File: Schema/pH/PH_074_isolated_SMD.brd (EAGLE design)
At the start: 67 x 48 mm, 31 parts, among them IC1 TL074D, IC2 TLC271D

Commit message: update pH schema and board
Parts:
- added R13: 1k, rcl:R1206W
- R8: device rcl:R0805W -> rcl:R1206W
- moved PWS1 11.4 mm to (64.7, 17.1), flipped to the top, turned to 180 degrees
- moved LED1 5.55 mm to (47.3, 7.80), turned to 180 degrees
- moved R6 5.40 mm to (47.3, 11.9)
- moved R5 5.40 mm to (45.2, 11.9)
- moved U$1 4.27 mm to (53.9, 23.2), turned to 270 degrees
- moved IL300 2.60 mm to (46.1, 26.3)
- moved TRIM1 1.00 mm to (35.5, 35.0)
- moved TRIM2 1.00 mm to (35.5, 13.0)
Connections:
- new net NIC: C7.1, IC2.6, R11.1, R13.2
- net GND: now also LED1.A
- net N$1: now also TRIM2.2; no longer TRIM2.1
- net N$12: now also TRIM1.2; no longer TRIM1.1
- net OUTPUT: now also R13.1; no longer C7.1, IC2.6, R11.1
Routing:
- net NIC: track 0.00 -> 16.8 mm
- net OUTPUT: track 19.9 -> 4.30 mm
- net +12V: track 90.6 -> 80.6 mm
- net +5V: track 16.8 -> 9.19 mm
- net N$1: track 26.7 -> 33.7 mm
- net N$7: track 35.4 -> 41.8 mm
- net -12V: track 49.6 -> 45.7 mm
- net N$8: track 10.7 -> 13.7 mm
- net N$21: track 23.4 -> 20.6 mm
- net N$9: track 5.70 -> 8.43 mm
- net N$12: track 21.1 -> 23.5 mm
- net N$4: track 19.8 -> 21.2 mm
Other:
- board text added: "+"
- board text added: "-"
- board text added: "GAIN"
- board text added: "OFFSET"
- board text added: "by Sensuino"
- board text added: "pH"
- board text added: "pH rev 1.1"

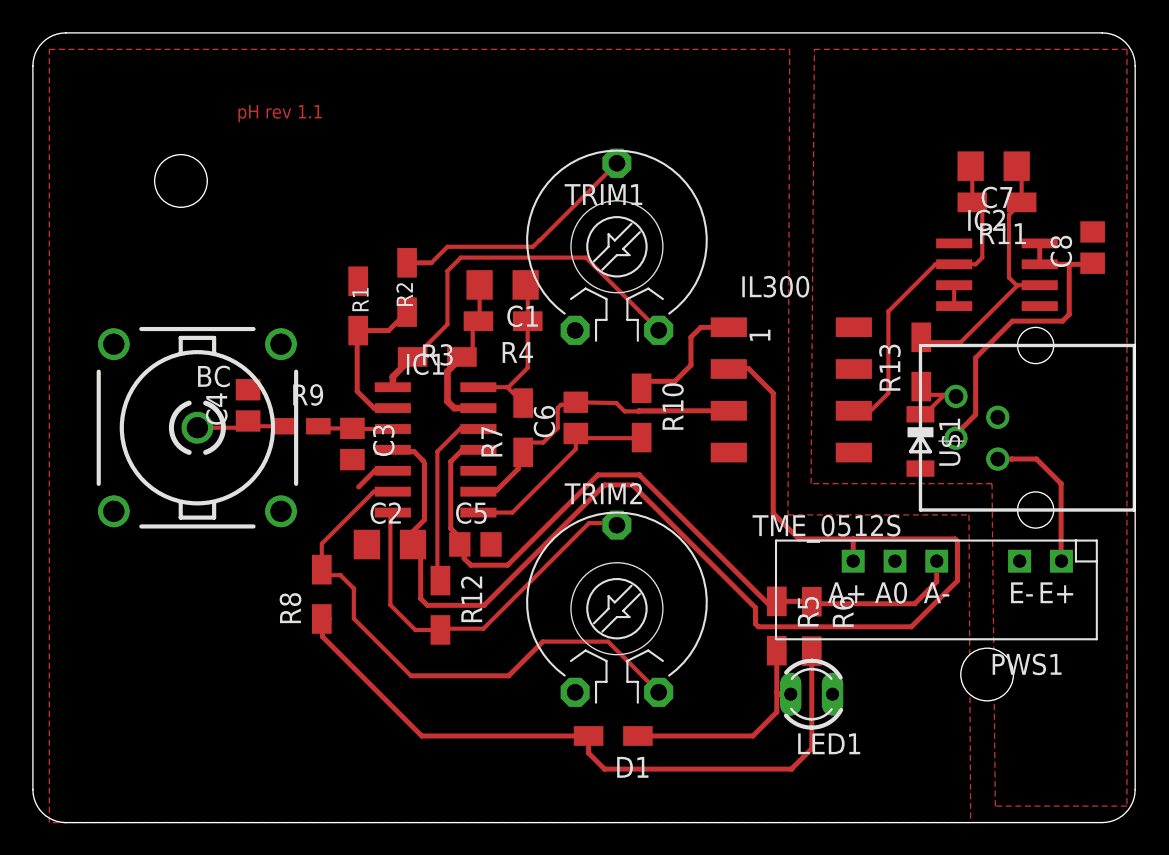
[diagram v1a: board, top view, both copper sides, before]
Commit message: little board adjustment
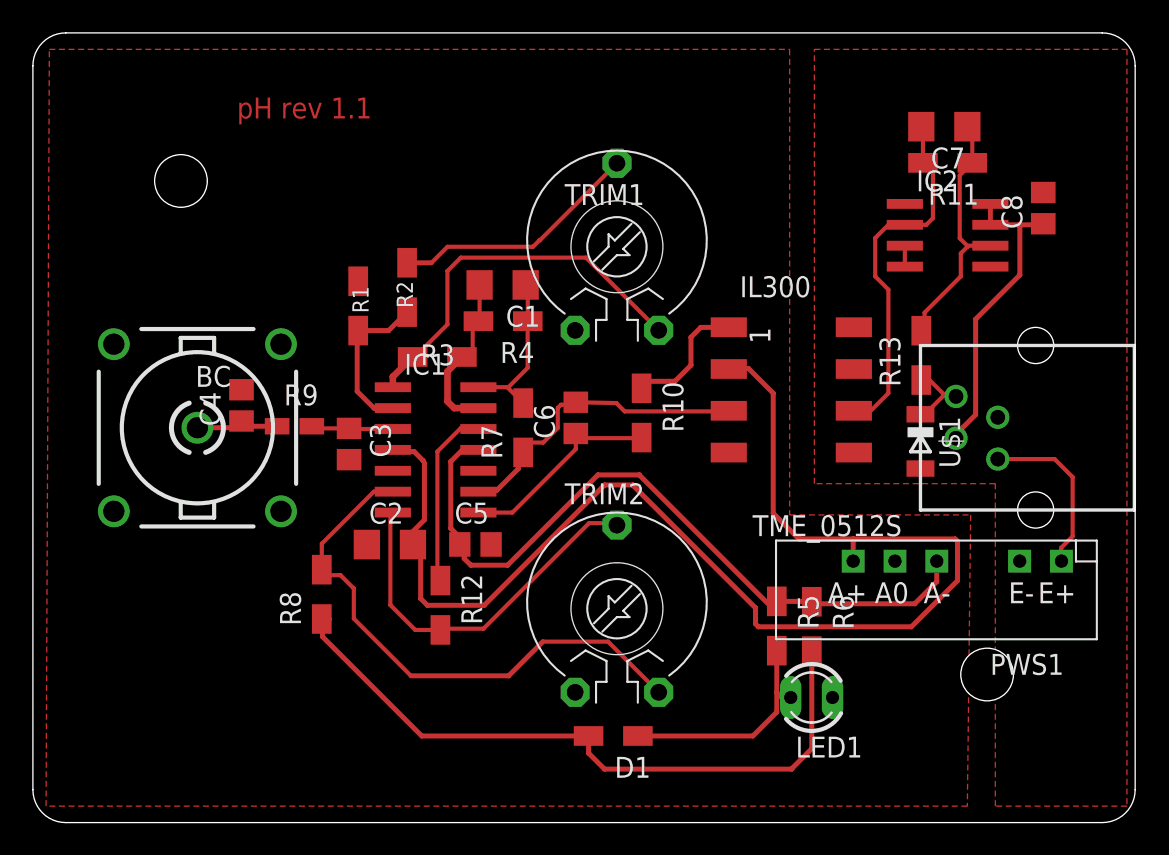
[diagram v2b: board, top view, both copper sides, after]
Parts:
- moved IC2 3.84 mm to (55.6, 35.7)
- moved C7 3.84 mm to (55.4, 42.3)
- moved C8 3.84 mm to (61.4, 37.4)
- moved R11 3.84 mm to (55.6, 40.1)
- moved C4 0.40 mm to (12.7, 25.4)
- moved R9 0.40 mm to (15.9, 24.1)
- moved R13 0.40 mm to (54.0, 28.4)
- moved C3 0.20 mm to (19.2, 23.0)
- moved LED1 0.20 mm to (47.3, 7.60)
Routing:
- net GND: track 2.61 -> 0.00 mm
- net N$21: track 20.6 -> 22.4 mm
- net N$4: track 21.2 -> 19.5 mm
- net +5V: track 9.19 -> 10.4 mm
- net VIN: track 19.7 -> 19.1 mm

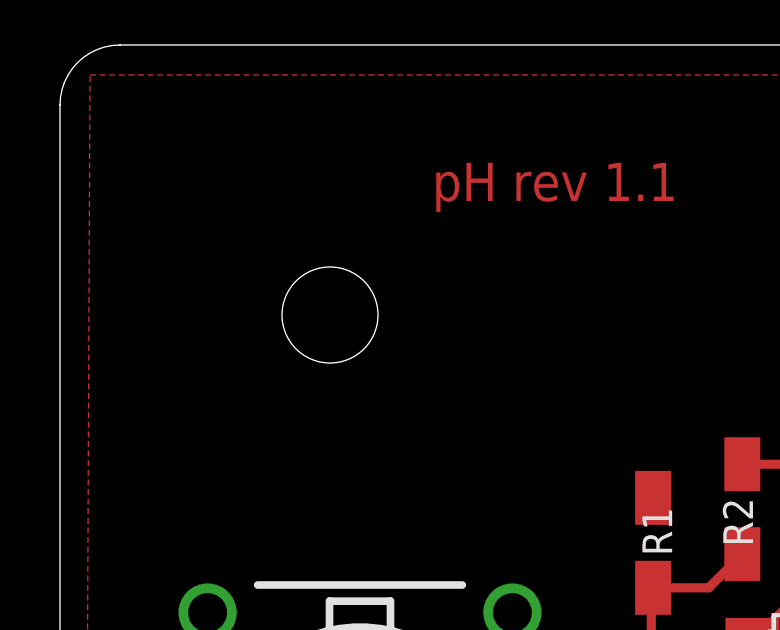
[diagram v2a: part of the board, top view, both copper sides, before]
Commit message: C3 and C4 corrected values
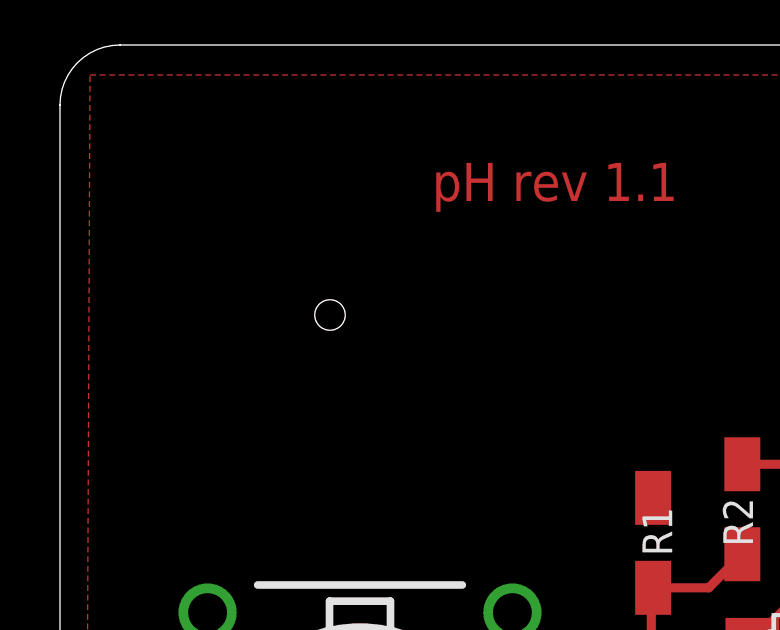
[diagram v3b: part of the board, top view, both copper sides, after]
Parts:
- C3: value 0.01uF -> 3.3pF
- C4: value 0.01uF -> 150pF
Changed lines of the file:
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@@
 <?xml version="1.0" encoding="utf-8"?>
 <!DOCTYPE eagle SYSTEM "eagle.dtd">
-<eagle version="6.4">
+<eagle version="6.6.0">
 <drawing>
 <settings>
@@
 <wire x1="65" y1="48" x2="2" y2="48" width="0" layer="20"/>
 <wire x1="2" y1="48" x2="0" y2="46" width="0" layer="20" curve="90"/>
-<hole x="9" y="39" drill="3.2"/>
+<hole x="9" y="39" drill="1.016"/>
 <hole x="58" y="9" drill="3.2"/>
 <wire x1="0" y1="2" x2="0" y2="46" width="0.4064" layer="30"/>
@@
 <element name="IC1" library="linear" package="SO14" value="TL074D" x="24.478" y="22.654" rot="R270"/>
 <element name="R9" library="rcl" package="R0805W" value="150k" x="15.9" y="24.09"/>
-<element name="C3" library="rcl" package="C0805" value="0.01uF" x="19.22" y="23.01" rot="R270"/>
-<element name="C4" library="rcl" package="C0805" value="0.01uF" x="12.68" y="25.36" rot="R90"/>
+<element name="C3" library="rcl" package="C0805" value="3.3pF" x="19.22" y="23.01" rot="R270"/>
+<element name="C4" library="rcl" package="C0805" value="150pF" x="12.68" y="25.36" rot="R90"/>
 <element name="R8" library="rcl" package="R1206W" value="3k3" x="17.5608" y="13.8736" rot="R90"/>
 <element name="D1" library="Sensuino" package="R1206W" value="1N4148" x="35.2752" y="5.264" smashed="yes" rot="R180">
